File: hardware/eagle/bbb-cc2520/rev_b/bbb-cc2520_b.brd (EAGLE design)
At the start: 54.6 x 86.4 mm, 69 parts, among them P1 MOLEX_73251-135X, P2 MOLEX_73251-135X, P9/P8 BBB_HEADERS, U1 CC2520, U2 CC2520, U3 CAT24C256WI-GT3, U4 CC2591, X1 NX2520SA, X2 NX2520SA

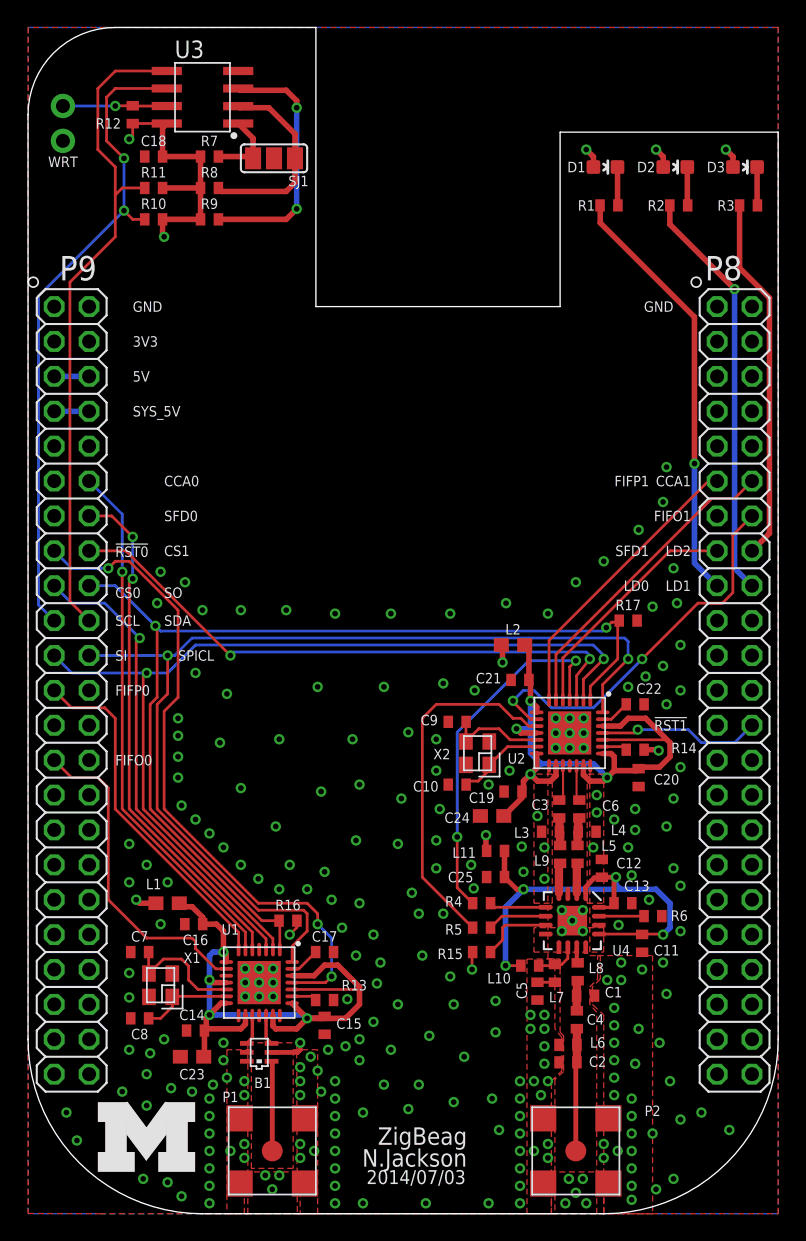
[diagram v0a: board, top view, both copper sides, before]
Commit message: revb mostly finished, need to add BLE chip
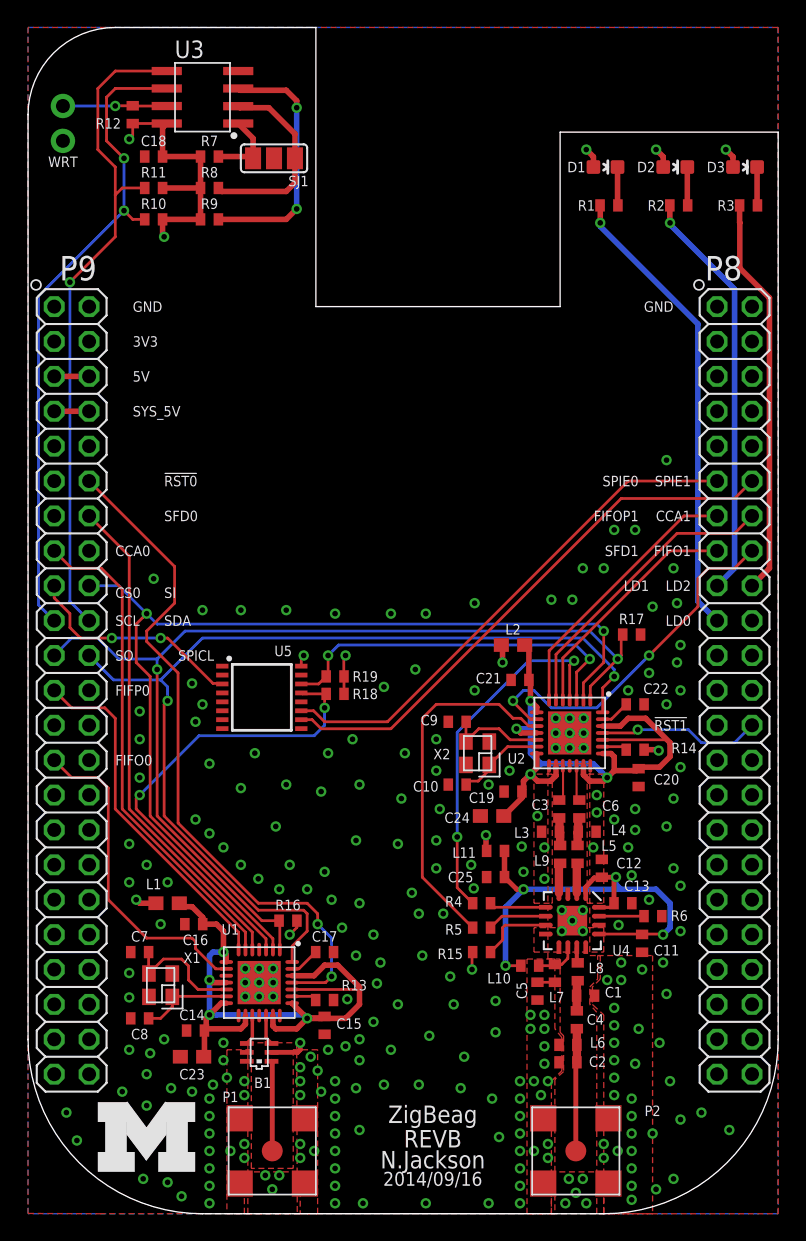
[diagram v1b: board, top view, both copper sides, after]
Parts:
- added R18, R19: 10k 1%, rcl:R0402
- added U5: CD4051B-53B, bbb-cc2520:TSSOP16
- moved R17 1.05 mm to (43.9, 42.2)
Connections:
- new net CS: P9/P8.P9_17, U5.3
- new net CS2: U5.15
- new net CS3: U5.12
- new net CS4: U5.1
- new net CS5: U5.5
- new net CS6: U5.2
- new net CS7: U5.4
- new net SPIE0: P9/P8.P8_11, U5.11
- new net SPIE1: P9/P8.P8_12, U5.10
- new net SPIE2: U5.9
- net !RESET0: now also P9/P8.P9_12; no longer P9/P8.P9_15
- net CCA0: now also P9/P8.P9_15; no longer P9/P8.P9_12
- net CCA1: now also P9/P8.P8_14; no longer P9/P8.P8_12
- net CS0: now also R18.1, U5.13; no longer P9/P8.P9_17
- net CS1: now also R19.1, U5.14; no longer P9/P8.P9_16
- net FIFO1: now also P9/P8.P8_16; no longer P9/P8.P8_14
- net FIFOP1: now also P9/P8.P8_13; no longer P9/P8.P8_11
- net GND: now also U5.6, U5.7, U5.8
- net LED0: now also P9/P8.P8_19; no longer P9/P8.P8_17
- net LED1: now also P9/P8.P8_17; no longer P9/P8.P8_18
- net LED2: now also P9/P8.P8_18; no longer P9/P8.P8_16
- net MISO: now also P9/P8.P9_21; no longer P9/P8.P9_18
- net MOSI: now also P9/P8.P9_18; no longer P9/P8.P9_21
- net VCC: now also R18.2, R19.2, U5.16
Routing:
- net SPIE1: track 0.00 -> 40.6 mm
- net SPIE0: track 0.00 -> 37.9 mm
- net CS1: track 43.4 -> 26.8 mm
- net CS: track 0.00 -> 16.3 mm, vias 0 -> 2
- net MOSI: track 69.7 -> 73.7 mm
- net VCC: track 30.3 -> 34.0 mm, vias 9 -> 11
- net SCLK: track 75.3 -> 72.2 mm
- net CCA0: track 38.8 -> 36.1 mm, vias 1 -> 0
- net LED2: track 26.6 -> 29.1 mm
- net LED0: track 31.2 -> 33.8 mm
- net FIFO1: track 28.8 -> 26.5 mm
- net !RESET0: track 48.5 -> 50.2 mm, vias 3 -> 2
- net FIFOP1: track 21.4 -> 19.9 mm
- net SFD0: track 37.7 -> 36.5 mm, vias 2 -> 0
- net CCA1: track 22.8 -> 21.8 mm
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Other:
- board text added: "2014/09/16"
- board text added: "FIFOP1"
- board text added: "REVB"
- board text added: "SPIE0"
- board text added: "SPIE1"
- board text removed: "2014/07/03"
- board text removed: "CS1"
- board text removed: "FIFP1"

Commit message: RevB finished
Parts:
- removed P1, P2: MOLEX_73251-135X, connector:SMA-J/PCB
- added ANT1, ANT2, ANT3: MOLEX_WM5544-ND, connector:MOLEX_WM5544-ND
- added B2: BAL-NRF01D3, chips:BAL-NRF01D3
- added C26: 0.1uF, passives:0402_CAP
- added C27, C32: 1nF, passives:0402_CAP
- added C28: 4.7uF, passives:0402_CAP
- added C29: 1uF, passives:0402_CAP
- added C30, C31: 12pF, passives:0402_CAP
- added C33: 47nF, passives:0402_CAP
- added C34: 2.2nF, passives:0402_CAP
- added C35: 0.8pF, passives:0402_CAP
- added D4: BLUE, SparkFun-LED:LED-0603
- added J1: TC2030-IDC, connector:TC2030-IDC
- added JP1: (no value), jumper:JP2Q
- added L12: (no value), passives:0402_CAP
- added L13: 10uH, passives:0603_CAP
- added R20, R21: 10k 1%, rcl:R0402
- added R22: 470, rcl:R0402
- added R23: 12k, passives:0603-RES
- added U6: NRF51822QF, chips:QFN-48-6MM
- added X3: 16MHz, crystals:TXC-8Y
- moved R18 8.64 mm to (14.7, 41.9)
- moved R19 1.27 mm to (22.4, 37.8)
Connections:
- removed net SPIE2: U5.9
- new net A0: U6.45
- new net A1: U6.46
- new net AVDD: C27.1, C29.1, L12.1, U6.35, U6.36
- new net BIRQ: P9/P8.P9_16, U6.11
- new net DCC: L13.2, U6.2
- new net N$36: B2.ANT1, U6.31
- new net N$37: B2.ANT2, U6.32
- new net N$38: ANT3.SIGNAL, B2.SE, C35.1
- new net N$39: L12.2, L13.1
- new net N$40: C30.1, U6.37, X3.1
- new net N$41: C31.1, U6.38, X3.3
- new net N$42: C32.1, U6.39
- new net N$43: C33.1, U6.29
- new net N$63: D4.A, R22.1
- new net N$64: R22.2, U6.19
- new net P03: JP1.1, U6.7
- new net P04: JP1.2, U6.8
- new net P05: JP1.4, U6.9
- new net P06: JP1.3, U6.10
- new net P12: U6.18
- new net P24: U6.43
- new net P25: U6.44
- new net PROG_RX: U6.47
- new net PROG_TX: U6.48
- new net SWDCLK: J1.4, R23.1, U6.24
- new net SWDIO: J1.2, U6.23
- new net VDD_PA: B2.VCC, C34.1, U6.30
- net CS0: now also R19.1; no longer R18.1
- net CS1: now also R20.1; no longer R19.1
- net CS2: now also R21.1, U6.17
- net CS4: now also R18.1
- net GND: now also ANT1.GND1, ANT1.GND2, ANT1.GND3, ANT1.GND4, ANT2.GND1, ANT2.GND2, ANT2.GND3, ANT2.GND4, ANT3.GND1, ANT3.GND2, ANT3.GND3, ANT3.GND4, B2.GND, C26.2, C27.2, C28.2, C29.2, C30.2, C31.2, C32.2, C33.2, C34.2, C35.2, D4.C, J1.5, R23.2, U5.9, U6.13, U6.33, U6.34, U6.GND; no longer P1.2, P1.3, P1.4, P1.5, P2.2, P2.3, P2.4, P2.5, P9/P8.P8_1
- net MISO: now also U6.15
- net MOSI: now also U6.14
- net N$52: now also ANT2.SIGNAL; no longer P2.1
- net N$7: now also ANT1.SIGNAL; no longer P1.1
- net SCLK: now also U6.16
- net VCC: now also C26.1, C28.1, J1.1, R20.2, R21.2, U6.1, U6.12
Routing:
- net N$64: track 0.00 -> 35.0 mm, vias 0 -> 2
- net BIRQ: track 0.00 -> 27.5 mm, vias 0 -> 1
- net SCLK: track 72.2 -> 99.6 mm, vias 2 -> 3
- net MISO: track 75.5 -> 102.4 mm, vias 2 -> 3
- net MOSI: track 73.7 -> 99.7 mm, vias 2 -> 3
- net CS2: track 0.00 -> 25.1 mm
- net VCC: track 34.0 -> 51.5 mm, vias 11 -> 13
- net AVDD: track 0.00 -> 17.1 mm, vias 0 -> 2
- net GND: track 5.76 -> 21.8 mm, vias 259 -> 272
- net SWDCLK: track 0.00 -> 12.7 mm
- net SWDIO: track 0.00 -> 12.0 mm
- net P05: track 0.00 -> 11.8 mm
- net P04: track 0.00 -> 11.7 mm
- net P06: track 0.00 -> 9.04 mm
- net P03: track 0.00 -> 8.97 mm
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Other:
- board text added: "P03"
- board text added: "P04"
- board text added: "P05"
- board text added: "P06"

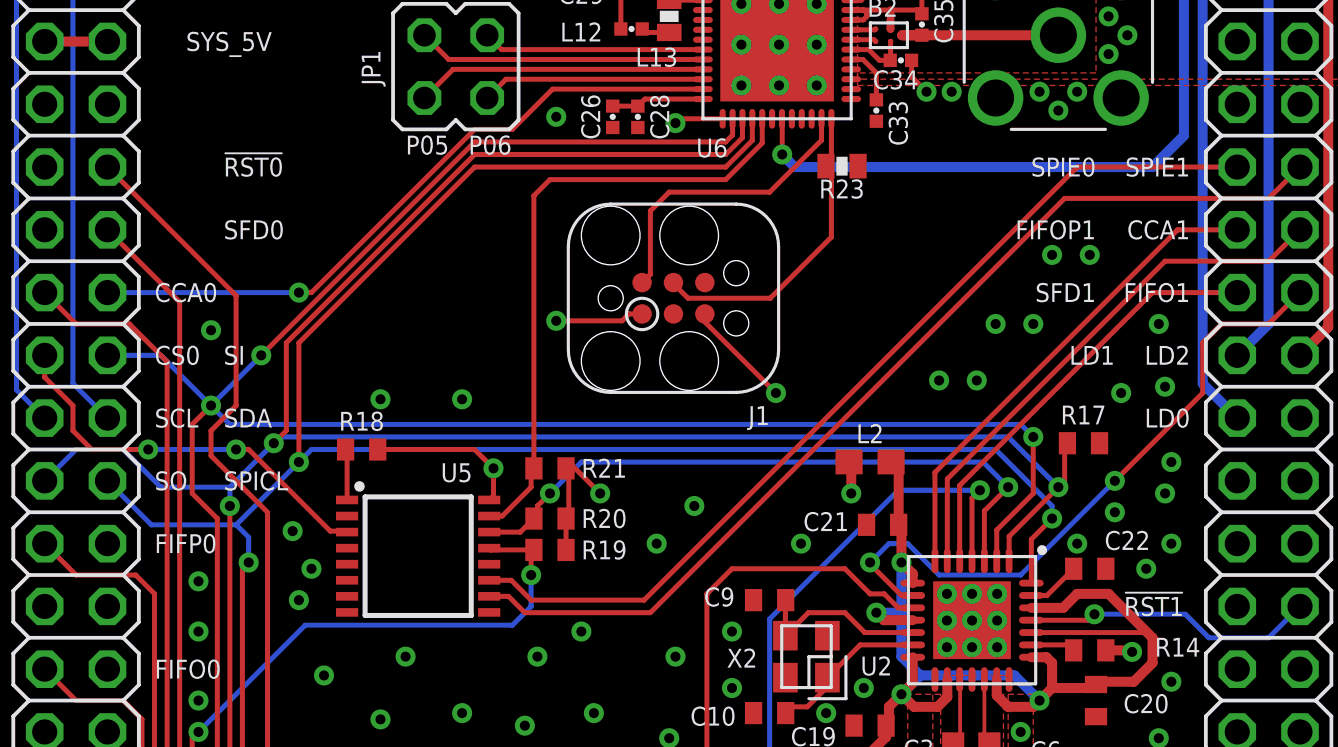
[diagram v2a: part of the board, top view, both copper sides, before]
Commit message: added label for bluetooth irq
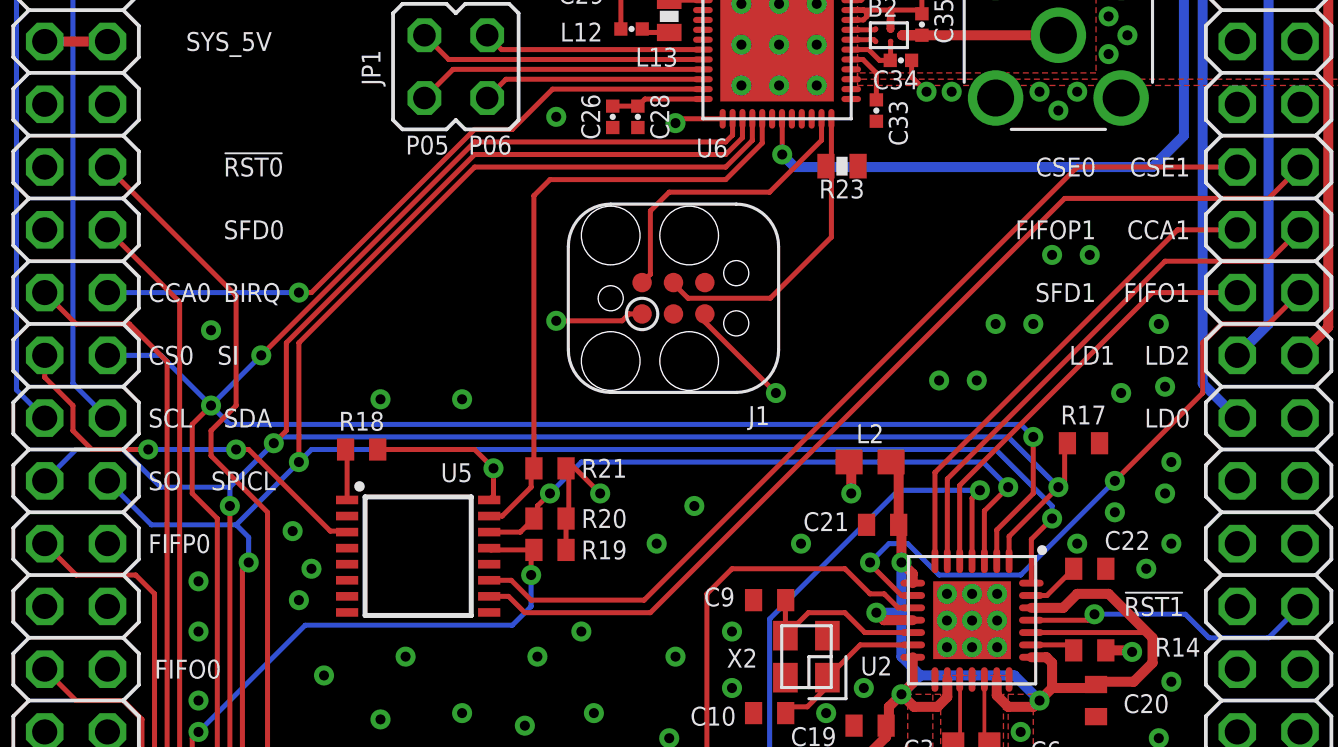
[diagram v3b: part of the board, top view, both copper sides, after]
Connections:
- net SPIE0 renamed CSE0
- net SPIE1 renamed CSE1
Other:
- board text added: "BIRQ"
- board text added: "CSE0"
- board text added: "CSE1"
- board text removed: "SPIE0"
- board text removed: "SPIE1"
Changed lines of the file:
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@@
 <setting verticaltext="up"/>
 </settings>
-<grid distance="0.05" unitdist="inch" unit="inch" style="lines" multiple="1" display="yes" altdistance="0.005" altunitdist="inch" altunit="inch"/>
+<grid distance="0.01" unitdist="inch" unit="inch" style="lines" multiple="1" display="yes" altdistance="0.005" altunitdist="inch" altunit="inch"/>
 <layers>
 <layer number="1" name="Top" color="4" fill="1" visible="yes" active="yes"/>
@@
 <text x="29.464" y="2.032" size="1.016" layer="21" font="vector" ratio="12" align="bottom-center">2014/09/16</text>
 <text x="29.464" y="6.604" size="1.27" layer="21" font="vector" ratio="14" align="bottom-center">ZigBeag</text>
-<text x="6.35" y="48.26" size="0.762" layer="25" font="vector" ratio="10" align="center-left">CCA0</text>
+<text x="6.096" y="48.26" size="0.762" layer="25" font="vector" ratio="10" align="center-left">CCA0</text>
 <text x="9.144" y="50.8" size="0.762" layer="25" font="vector" ratio="10" align="center-left">SFD0</text>
 <text x="9.144" y="53.34" size="0.762" layer="25" font="vector" ratio="10" align="center-left">!RST0</text>
-<text x="6.35" y="45.72" size="0.762" layer="25" font="vector" ratio="10" align="center-left">CS0</text>
-<text x="9.144" y="45.72" size="0.762" layer="25" font="vector" ratio="10" align="center-left">SI</text>
+<text x="6.096" y="45.72" size="0.762" layer="25" font="vector" ratio="10" align="center-left">CS0</text>
+<text x="8.89" y="45.72" size="0.762" layer="25" font="vector" ratio="10" align="center-left">SI</text>
 <text x="9.144" y="43.18" size="0.762" layer="25" font="vector" ratio="10" align="center-left">SDA</text>
 <text x="7.62" y="66.04" size="0.762" layer="25" font="vector" ratio="10" align="center-left">GND</text>
@@
 <text x="7.62" y="60.96" size="0.762" layer="25" font="vector" ratio="10" align="center-left">5V</text>
 <text x="7.62" y="58.42" size="0.762" layer="25" font="vector" ratio="10" align="center-left">SYS_5V</text>
-<text x="6.35" y="43.18" size="0.762" layer="25" font="vector" ratio="10" align="center-left">SCL</text>
-<text x="6.35" y="40.64" size="0.762" layer="25" font="vector" ratio="10" align="center-left">SO</text>
-<text x="9.144" y="40.64" size="0.762" layer="25" font="vector" ratio="10" align="center-left">SPICL</text>
-<text x="6.35" y="38.1" size="0.762" layer="25" font="vector" ratio="10" align="center-left">FIFP0</text>
+<text x="6.096" y="43.18" size="0.762" layer="25" font="vector" ratio="10" align="center-left">SCL</text>
+<text x="6.096" y="40.64" size="0.762" layer="25" font="vector" ratio="10" align="center-left">SO</text>
+<text x="8.636" y="40.64" size="0.762" layer="25" font="vector" ratio="10" align="center-left">SPICL</text>
+<text x="6.096" y="38.1" size="0.762" layer="25" font="vector" ratio="10" align="center-left">FIFP0</text>
 <text x="6.35" y="33.02" size="0.762" layer="25" font="vector" ratio="10" align="center-left">FIFO0</text>
 <text x="46.99" y="66.04" size="0.762" layer="25" font="vector" ratio="10" align="center-right">GND</text>
-<text x="44.45" y="53.34" size="0.762" layer="25" font="vector" ratio="10" align="center-right">SPIE0</text>
-<text x="48.26" y="53.34" size="0.762" layer="25" font="vector" ratio="10" align="center-right">SPIE1</text>
+<text x="44.45" y="53.34" size="0.762" layer="25" font="vector" ratio="10" align="center-right">CSE0</text>
+<text x="48.26" y="53.34" size="0.762" layer="25" font="vector" ratio="10" align="center-right">CSE1</text>
 <text x="48.26" y="50.8" size="0.762" layer="25" font="vector" ratio="10" align="center-right">CCA1</text>
 <text x="48.26" y="48.26" size="0.762" layer="25" font="vector" ratio="10" align="center-right">FIFO1</text>
@@
 <text x="16.51" y="54.61" size="0.762" layer="25" font="vector" ratio="10" align="top-left">P05</text>
 <text x="19.05" y="54.61" size="0.762" layer="25" font="vector" ratio="10" align="top-left">P06</text>
+<text x="9.144" y="48.26" size="0.762" layer="25" font="vector" ratio="10" align="center-left">BIRQ</text>
 </plain>
 <attributes>
@@
 <wire x1="14.102" y1="38.608" x2="14.143" y2="38.567" width="0.2032" layer="1"/>
 </signal>
-<signal name="SPIE0">
-<contactref element="U5" pad="11"/>
-<contactref element="P9/P8" pad="P8_11"/>
-<wire x1="19.893" y1="36.617" x2="20.787" y2="36.617" width="0.2032" layer="1"/>
-<wire x1="20.787" y1="36.617" x2="21.59" y2="35.814" width="0.2032" layer="1"/>
-<wire x1="21.59" y1="35.814" x2="26.162" y2="35.814" width="0.2032" layer="1"/>
-<wire x1="50.165" y1="53.34" x2="43.688" y2="53.34" width="0.2032" layer="1"/>
-<wire x1="43.688" y1="53.34" x2="26.162" y2="35.814" width="0.2032" layer="1"/>
-</signal>
 <signal name="CS2">
 <contactref element="U5" pad="15"/>
@@
 <signal name="CS3">
 <contactref element="U5" pad="12"/>
-</signal>
-<signal name="SPIE1">
-<contactref element="U5" pad="10"/>
-<contactref element="P9/P8" pad="P8_12"/>
-<wire x1="19.893" y1="35.967" x2="20.675" y2="35.967" width="0.2032" layer="1"/>
-<wire x1="20.675" y1="35.967" x2="21.336" y2="35.306" width="0.2032" layer="1"/>
-<wire x1="21.336" y1="35.306" x2="26.416" y2="35.306" width="0.2032" layer="1"/>
-<wire x1="26.416" y1="35.306" x2="43.18" y2="52.07" width="0.2032" layer="1"/>
-<wire x1="43.18" y1="52.07" x2="51.435" y2="52.07" width="0.2032" layer="1"/>
-<wire x1="51.435" y1="52.07" x2="52.705" y2="53.34" width="0.2032" layer="1"/>
 </signal>
 <signal name="CS5">
@@
 <wire x1="20.393" y1="58.093" x2="19.812" y2="58.674" width="0.2032" layer="1"/>
 </signal>
+<signal name="CSE0">
+<contactref element="U5" pad="11"/>
+<contactref element="P9/P8" pad="P8_11"/>
+<wire x1="20.787" y1="36.617" x2="21.59" y2="35.814" width="0.2032" layer="1"/>
+<wire x1="21.59" y1="35.814" x2="26.162" y2="35.814" width="0.2032" layer="1"/>
+<wire x1="50.165" y1="53.34" x2="43.688" y2="53.34" width="0.2032" layer="1"/>
+<wire x1="43.688" y1="53.34" x2="26.162" y2="35.814" width="0.2032" layer="1"/>
+<wire x1="20.787" y1="36.617" x2="19.893" y2="36.617" width="0.2032" layer="1"/>
+</signal>
+<signal name="CSE1">
+<contactref element="U5" pad="10"/>
+<contactref element="P9/P8" pad="P8_12"/>
+<wire x1="20.675" y1="35.967" x2="21.336" y2="35.306" width="0.2032" layer="1"/>
+<wire x1="21.336" y1="35.306" x2="26.416" y2="35.306" width="0.2032" layer="1"/>
+<wire x1="26.416" y1="35.306" x2="43.18" y2="52.07" width="0.2032" layer="1"/>
+<wire x1="43.18" y1="52.07" x2="51.435" y2="52.07" width="0.2032" layer="1"/>
+<wire x1="51.435" y1="52.07" x2="52.705" y2="53.34" width="0.2032" layer="1"/>
+<wire x1="20.675" y1="35.967" x2="19.893" y2="35.967" width="0.2032" layer="1"/>
+</signal>
 </signals>
